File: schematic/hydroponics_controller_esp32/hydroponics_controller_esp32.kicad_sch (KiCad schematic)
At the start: 27 parts, among them J1 12v -, J10 RJ45, J11 5v-16v in, J12 DC 12V Relay Module 4 Ch with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, J13 Conn_01x04_Pin, J14 Conn_01x04_Pin, J2 12v +, J3 RJ45, J4 Power Input, J5 Flow Meters, J8 ADS1115 16 Bit 4 Channel I2C, M1 Dose_A, M2 Dose_B, SW1 Fill Solinoid, U1 DS18B20, U10 Flow East, U11 Flow West, U12 Flow Fill, U2 HXZ11, U4 TDS Meter, U5 Load Cell, U7 Load Cell, U8 Load Cell, U9 0-5v

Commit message: Standardized Package files for hydro
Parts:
- U2: value HXZ11 -> HX711
- U3, U6: value ~ -> (none)
- U4: value TDS Meter -> KEYESTUDIO TDS Meter Probe
- U9: value 0-5v -> Alternate Level Sensor
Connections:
- net at J3.1 (3v3), U1.3 (V_{DD}), U2. (GND): now also R1.2
- net at J3.2 (GND), U1.1 (GND), U2. (GND): no longer R1.2
- net at U6. (Blk): now also U5. (Blk); no longer U2. (GND)
- net at U8. (Blk): now also U7. (Blk); no longer U6. (Blk)
- net at U5. (Blk): now also U7. (Blk); no longer U6. (Blk)
- net at J5.3 (Pin_3), U10. (3.3v), U3.8 (D25_GPIO25): no longer J5.4 (Pin_4), U11. (3.3v), U3.24 (D18_GPIO18)
- net at J13.5v, J8.1 (VCC), U4. (SIG)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: no longer J12.1 (VCC)
- net at J12.3 (IN1): now also U3.6 (D32_GPIO32)
- net at J12.6 (IN4): now also U3.10 (D27_GPIO27)
- net at J10.1 (3v3), J13.3v3, J4.3V3: now also J5.2 (Pin_2), U10. (3.3v), U11. (3.3v), U12. (3.3v)
- net at J11.1, J2.6 (Pin_6): now also J12.1 (VCC)
- net at U2. (GND): now also U5. (Blk)
- net at J8.8 (A1), U9.3 (Vout): no longer J8.7 (A0), U4. (SIG)
- net at J10.6 (DT), U3.30 (D23_GPIO23): no longer J10.7 (DQ), U3.9 (D26_GPIO26)
- new net: U2. (GND), U6. (Blk)
- new net: U6. (Blk), U8. (Blk)
- new net: J10.2 (GND), J14.GND, J4.GND, J5.1 (Pin_1), J8.2 (GND), U10. (3.3v), U11. (3.3v), U12. (3.3v), U4. (SIG)
- new net: J5.4 (Pin_4), U11. (3.3v), U3.24 (D18_GPIO18)
- new net: J12.2 (GND), J14.GND, U9.1 (GND)
- new net: J12.4 (IN2), U3.7 (D33_GPIO33)
- new net: J12.5 (IN3), U3.11 (D14_GPIO14)
- new net: U2. (GND), U7. (Blk)
- new net: U2. (GND), U8. (Blk)
- new net: J8.7 (A0), U4. (SIG)
- new net: J10.7 (DQ), U3.9 (D26_GPIO26)
- now unconnected: J14.GND, J14.GND, U4. (SIG)

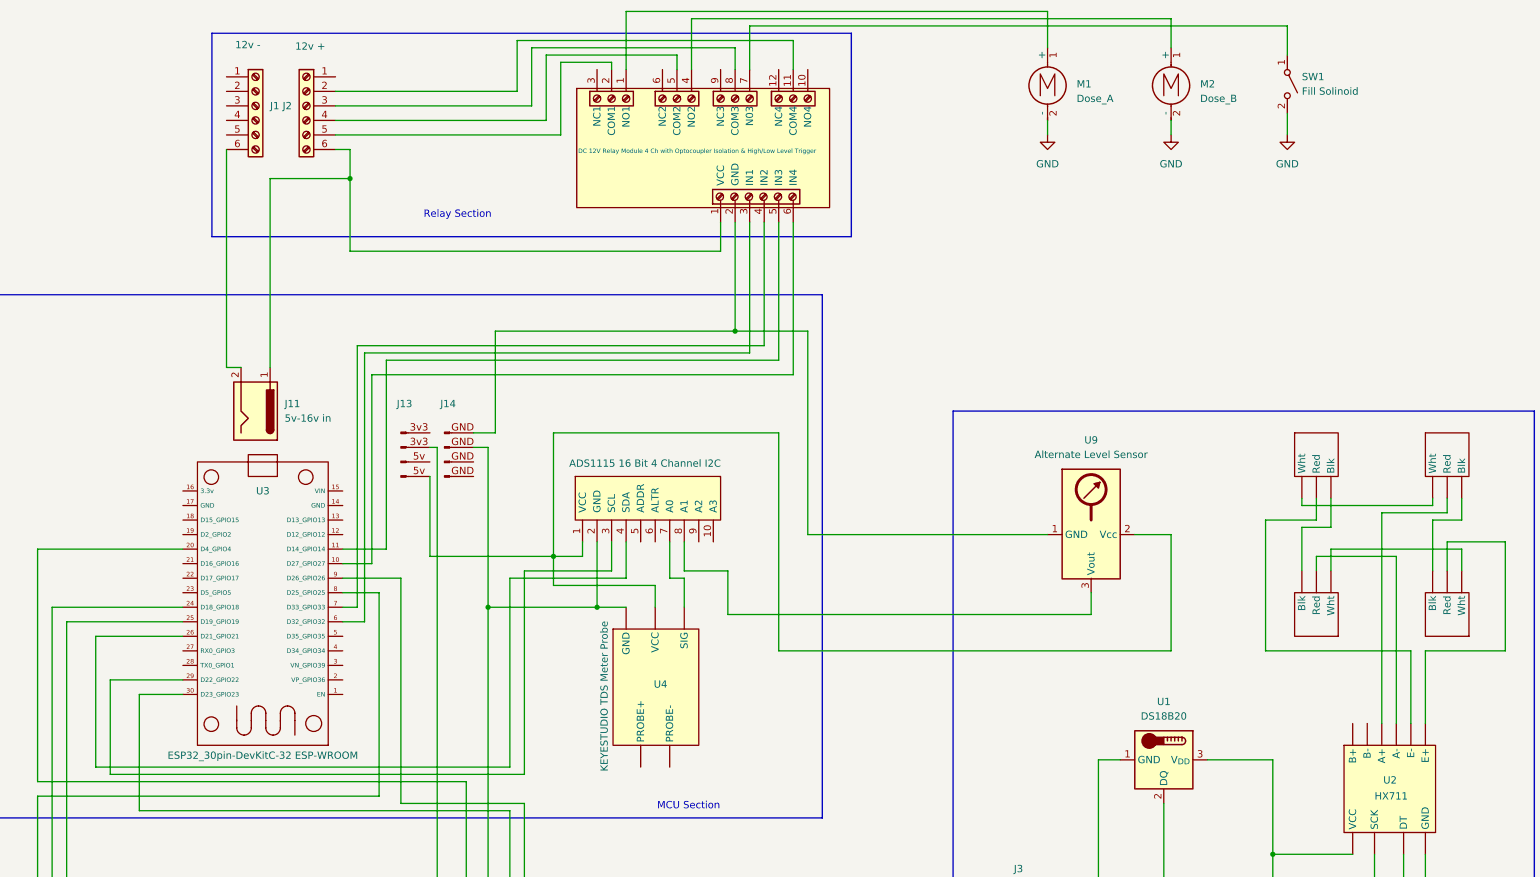
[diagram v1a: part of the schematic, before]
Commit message: feat: add EC reference history dashboard and calibration workflow
Implemented a dedicated EC Reference History dashboard integrated with the Hydro-History Browser.

Highlights:
- Added Node-RED EC Reference History query branch.
- Published formatted EC reference history to MQTT.
- Added Home Assistant MQTT sensor and Markdown dashboard card.
- Added rainfall and estimated dilution context to EC reference history.
- Added operator note support for engineering observations.
- Improved formatting for null values in historical records.
- Updated dashboard history design documentation to reflect production implementation.
- Corrected ADS1115 hardware configuration by powering the ADC from the 3.3V rail while retaining the TDS module at 5V.
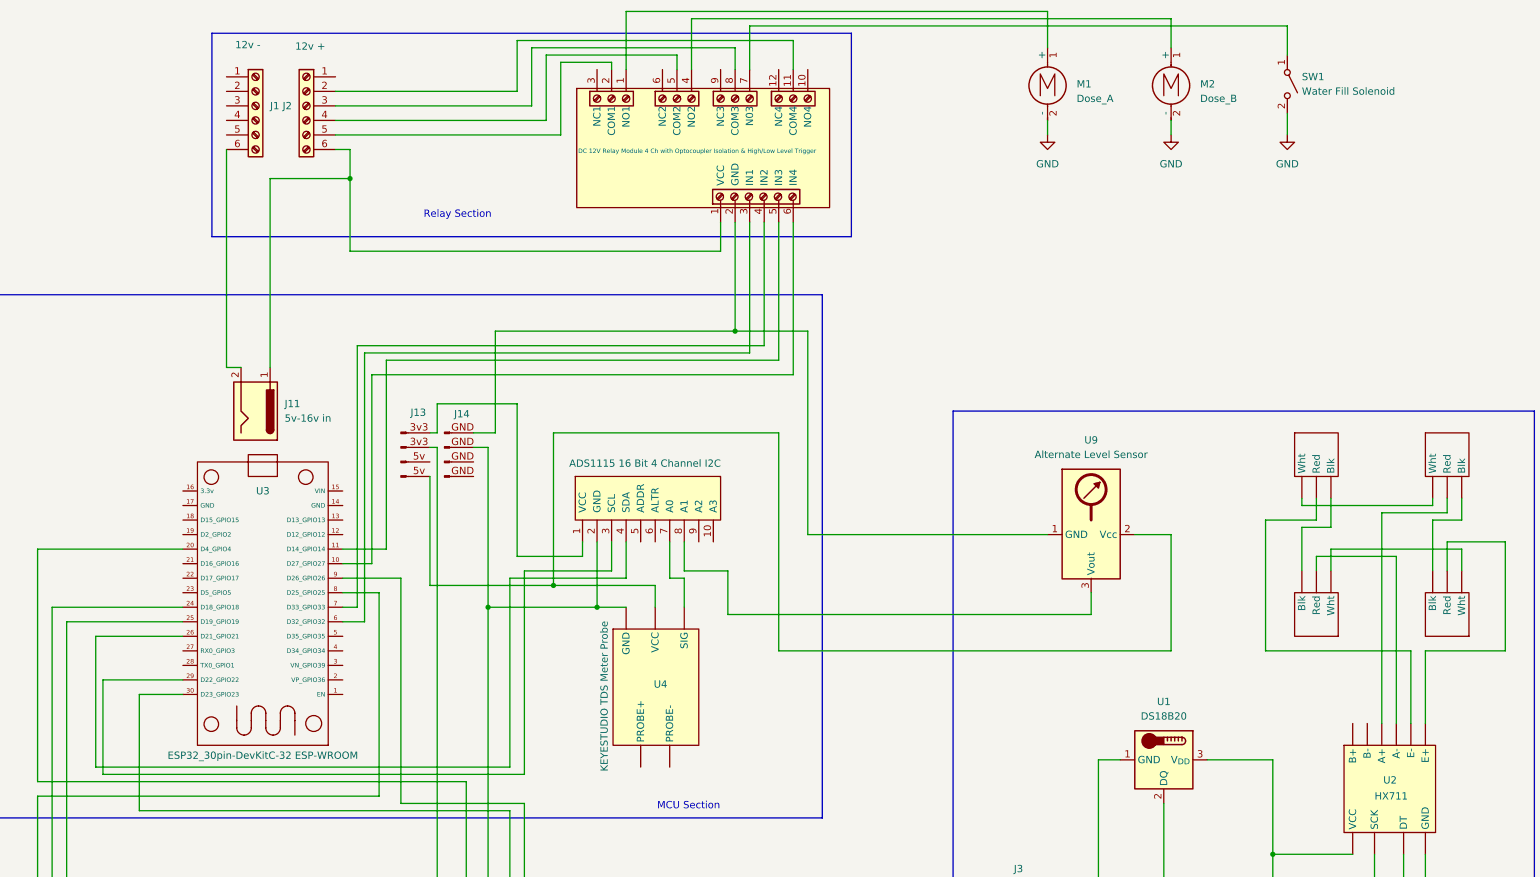
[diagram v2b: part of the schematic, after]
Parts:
- SW1: value Fill Solinoid -> Water Fill Solenoid
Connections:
- net at U6. (Blk): now also U5. (Blk); no longer U2. (GND)
- net at U8. (Blk): now also U7. (Blk); no longer U6. (Blk)
- net at U5. (Blk): now also U7. (Blk); no longer U6. (Blk)
- net at J12.3 (IN1): now also U3.6 (D32_GPIO32)
- net at J12.6 (IN4): now also U3.10 (D27_GPIO27)
- net at J13.3v3: now also J8.1 (VCC)
- net at J13.5v: now also U4. (SIG), U9.2 (Vcc)
- net at U2. (GND): now also U5. (Blk)
- new net: U2. (GND), U6. (Blk)
- new net: U6. (Blk), U8. (Blk)
- new net: J10.2 (GND), J14.GND, J4.GND, J5.1 (Pin_1), J8.2 (GND), U10. (3.3v), U11. (3.3v), U12. (3.3v), U4. (SIG)
- new net: J10.1 (3v3), J13.3v3, J4.3V3, J5.2 (Pin_2), U10. (3.3v), U11. (3.3v), U12. (3.3v)
- new net: J12.2 (GND), J14.GND, U9.1 (GND)
- new net: U2. (GND), U7. (Blk)
- new net: U2. (GND), U8. (Blk)
- now unconnected: J14.GND, J14.GND, U4. (SIG), U4. (SIG)
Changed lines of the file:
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@@
 		(rev "2")
 		(company "Engineering Innovations, LLC")
+		(comment 1 "Updated 7/3/26")
 	)
 	(rectangle
@@
 	)
 	(junction
+		(at 118.11 119.38)
+		(diameter 0)
+		(color 0 0 0 0)
+	)
+	(junction
 		(at 95.25 196.85)
 		(diameter 0)
@@
 	)
 	(junction
-		(at 118.11 114.3)
-		(diameter 0)
-		(color 0 0 0 0)
-	)
-	(junction
 		(at 106.68 123.19)
 		(diameter 0)
@@
 	(wire
 		(pts
-			(xy 40.64 135.89) (xy 53.34 135.89)
+			(xy 111.76 114.3) (xy 111.76 87.63)
+		)
+		(stroke
+			(width 0)
+			(type default)
+			(color 255 0 0 1)
+		)
+	)
+	(wire
+		(pts
+			(xy 39.37 135.89) (xy 53.34 135.89)
 		)
 		(stroke
@@
 	(wire
 		(pts
-			(xy 123.19 114.3) (xy 118.11 114.3)
-		)
-		(stroke
-			(width 0)
-			(type default)
-			(color 132 0 0 1)
-		)
-	)
-	(wire
-		(pts
 			(xy 251.46 114.3) (xy 265.43 114.3)
 		)
@@
 	(wire
 		(pts
-			(xy 85.09 78.74) (xy 85.09 125.73)
+			(xy 96.52 119.38) (xy 118.11 119.38)
 		)
 		(stroke
 			(width 0)
 			(type default)
-			(color 0 0 194 1)
+			(color 132 0 0 1)
 		)
 	)
 	(wire
 		(pts
-			(xy 30.48 123.19) (xy 53.34 123.19)
+			(xy 85.09 78.74) (xy 85.09 125.73)
 		)
 		(stroke
 			(width 0)
 			(type default)
-			(color 194 0 0 1)
+			(color 0 0 194 1)
 		)
 	)
 	(wire
 		(pts
-			(xy 96.52 114.3) (xy 118.11 114.3)
+			(xy 30.48 123.19) (xy 53.34 123.19)
 		)
 		(stroke
 			(width 0)
 			(type default)
-			(color 132 0 0 1)
+			(color 194 0 0 1)
 		)
 	)
@@
 			(width 0)
 			(type default)
-			(color 132 0 0 1)
+			(color 255 0 0 1)
 		)
 	)
@@
 	(wire
 		(pts
-			(xy 96.52 114.3) (xy 96.52 100.33)
-		)
-		(stroke
-			(width 0)
-			(type default)
-			(color 132 0 0 1)
-		)
-	)
-	(wire
-		(pts
 			(xy 246.38 21.59) (xy 246.38 26.67)
 		)
@@
 			(width 0)
 			(type default)
+			(color 255 0 0 1)
 		)
 	)
@@
 	(wire
 		(pts
+			(xy 97.79 92.71) (xy 96.52 92.71)
+		)
+		(stroke
+			(width 0)
+			(type default)
+			(color 255 0 0 1)
+		)
+	)
+	(wire
+		(pts
 			(xy 53.34 113.03) (xy 27.94 113.03)
 		)
@@
 	(wire
 		(pts
-			(xy 40.64 152.4) (xy 40.64 135.89)
+			(xy 39.37 152.4) (xy 39.37 135.89)
 		)
 		(stroke
@@
 	(wire
 		(pts
+			(xy 96.52 100.33) (xy 96.52 119.38)
+		)
+		(stroke
+			(width 0)
+			(type default)
+			(color 132 0 0 1)
+		)
+	)
+	(wire
+		(pts
 			(xy 162.56 110.49) (xy 204.47 110.49)
 		)
@@
 	(wire
 		(pts
-			(xy 113.03 152.4) (xy 40.64 152.4)
+			(xy 113.03 152.4) (xy 39.37 152.4)
 		)
 		(stroke
@@
 	(wire
 		(pts
+			(xy 111.76 87.63) (xy 97.79 87.63)
+		)
+		(stroke
+			(width 0)
+			(type default)
+			(color 255 0 0 1)
+		)
+	)
+	(wire
+		(pts
 			(xy 243.84 166.37) (xy 243.84 194.31)
 		)
@@
 	(wire
 		(pts
+			(xy 97.79 87.63) (xy 97.79 92.71)
+		)
+		(stroke
+			(width 0)
+			(type default)
+			(color 255 0 0 1)
+		)
+	)
+	(wire
+		(pts
 			(xy 107.95 196.85) (xy 110.49 196.85)
 		)
@@
 	(wire
 		(pts
-			(xy 118.11 114.3) (xy 118.11 92.71)
-		)
-		(stroke
-			(width 0)
-			(type default)
-			(color 132 0 0 1)
-		)
-	)
-	(wire
-		(pts
 			(xy 106.68 95.25) (xy 106.68 123.19)
 		)
@@
 	(wire
 		(pts
+			(xy 111.76 114.3) (xy 123.19 114.3)
+		)
+		(stroke
+			(width 0)
+			(type default)
+			(color 255 0 0 1)
+		)
+	)
+	(wire
+		(pts
 			(xy 128.27 27.94) (xy 128.27 29.21)
 		)
@@
 	(wire
 		(pts
-			(xy 118.11 119.38) (xy 118.11 114.3)
+			(xy 118.11 92.71) (xy 118.11 119.38)
 		)
 		(stroke
@@
 			)
 		)
-		(property "Value" "Fill Solinoid"
+		(property "Value" "Water Fill Solenoid"
 			(at 248.92 33.0199 90)
 			(show_name no)
@@
 		(dnp no)
 		(property "Reference" "J13"
-			(at 92.075 87.63 0)
+			(at 94.488 89.154 0)
 			(show_name no)
 			(do_not_autoplace no)
@@
 		(dnp no)
 		(property "Reference" "J14"
-			(at 99.695 87.63 0)
+			(at 102.108 89.408 0)
 			(show_name no)
 			(do_not_autoplace no)

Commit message: Hydroponics: Begin persistent fill-cycle state architecture
- Removed legacy Auto Fill notification and CSV logging
- Simplified Auto Fill completion automation
- Fixed ESPHome helper naming (outside_tank_* entities)
- Added persistent last-fill gallons helper
- Added read-only controller display sensors
- Updated Flow-1 notification to report starting and final fill volumes
- Reorganized controller dashboard terminology
- Added engineering log for 2026-07-04 validation and debugging
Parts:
- added TP1: EC Tank Probe, symbol Connector:TestPoint_2Pole
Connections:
- net at U6. (Blk): now also U5. (Blk); no longer U2. (GND)
- net at U8. (Blk): now also U7. (Blk); no longer U6. (Blk)
- net at U5. (Blk): now also U7. (Blk); no longer U6. (Blk)
- net at J12.3 (IN1): now also U3.6 (D32_GPIO32)
- net at J12.6 (IN4): now also U3.10 (D27_GPIO27)
- net at J13.5v: now also U4. (SIG), U9.2 (Vcc)
- net at U2. (GND): now also U5. (Blk)
- net at U4. (SIG): now also TP1.2
- new net: U2. (GND), U6. (Blk)
- new net: U6. (Blk), U8. (Blk)
- new net: J10.2 (GND), J14.GND, J4.GND, J5.1 (Pin_1), J8.2 (GND), U10. (3.3v), U11. (3.3v), U12. (3.3v), U4. (SIG)
- new net: J10.1 (3v3), J13.3v3, J4.3V3, J5.2 (Pin_2), U10. (3.3v), U11. (3.3v), U12. (3.3v)
- new net: J12.2 (GND), J14.GND, U9.1 (GND)
- new net: U2. (GND), U7. (Blk)
- new net: U2. (GND), U8. (Blk)
- new net: TP1.1, U4. (SIG)
- now unconnected: J14.GND, J14.GND
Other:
- note added: "Controller Reference Applies to Hardware Revision 2 ESP32 DevKitC-32 (30-pin) ESPHome 2025.7.2 | DevKit | GPIO | KiCad Pin | Signal Path | | -------| -------| --------- | --------------------------------------- | | D32 | GPIO32 | Pin 6 | Relay IN1 → NO1 → Dose Pump A | | D33 | GPIO33 | Pin 7 | Relay IN2 → NO2 → Dose Pump B | | D14 | GPIO14 | Pin 11 | Relay IN3 → NO3 → Water Fill Solenoid | | D27 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"
- note added: "Perf Board Section"
- note added: "Possible Future"
- note added: "Scale Sensor Layout"
- note added: "Tank Water Temp"
- note removed: "PCB Section"
- moved on the sheet: J10, J3, J4, J5, U1, U10, U11, U12, U2, U9
